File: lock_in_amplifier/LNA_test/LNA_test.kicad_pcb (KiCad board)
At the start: 2 copper layers, 22.1 x 17.8 mm, 111 parts, among them J1 vref-in, J10 A IN, J11 B IN, J12 POWER_IN, J15 I IN, J17 RF_Shield_One_Piece, J19 +3V3 OUT, J2 vref, J20 AMP OUT, J3 V-IN, J38 RF_Shield_One_Piece, J4 GND, J46 -5V OUT, J47 +5V OUT, J5 V+IN, J6 +5V, J7 +3V3, J8 -5V, Q1 DMN640L, Q2 DMN640L, U1 LM833, U2 lm7805, U3 LM7833, U4 lm7905, U6 lmp7721, U7 LM833, U8 AD8429

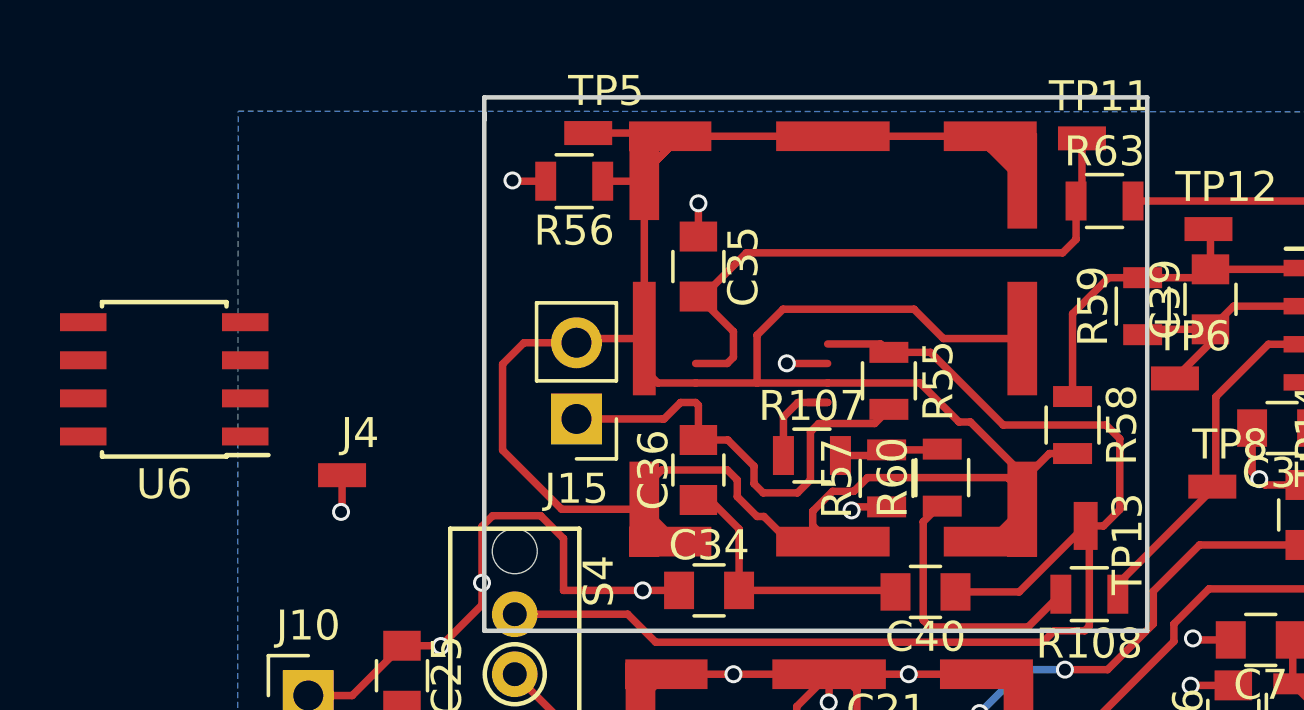
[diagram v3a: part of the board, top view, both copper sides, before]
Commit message: finished relayout of tia - soic
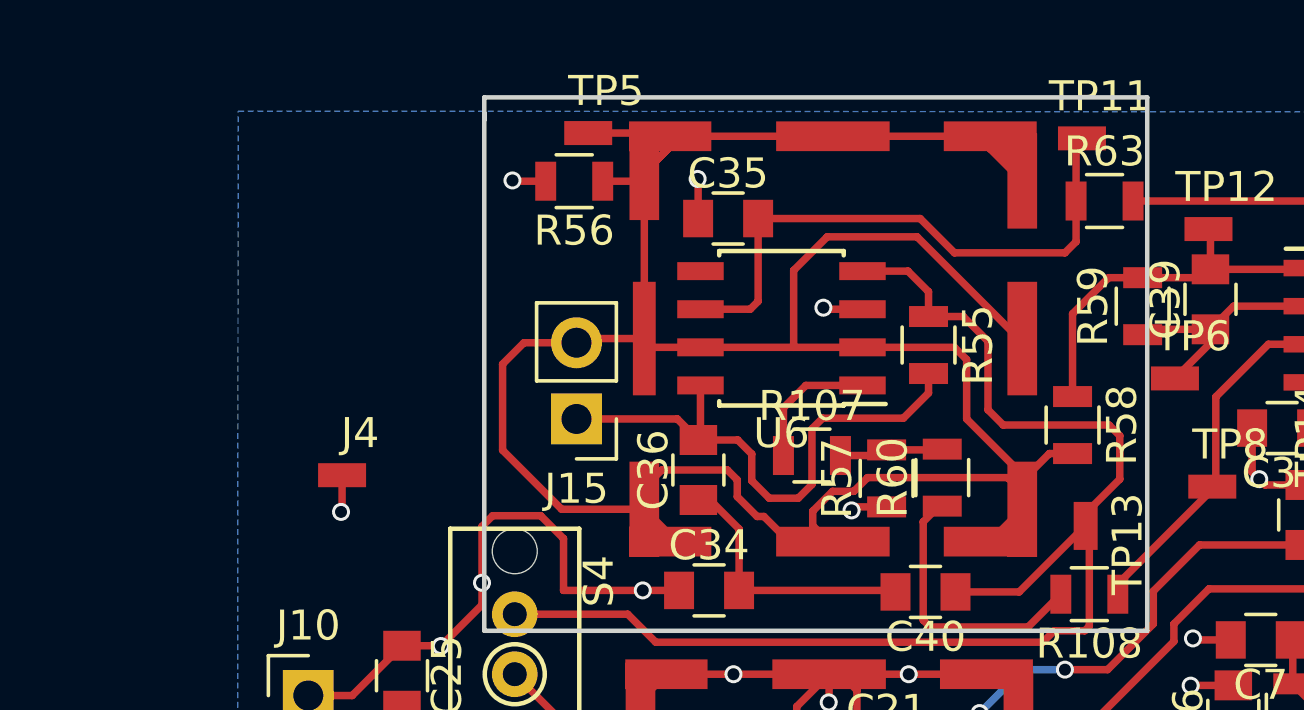
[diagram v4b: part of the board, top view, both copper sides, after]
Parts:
- moved U6 20.6 mm to (101.1, 70.4)
- moved C35 1.88 mm to (99.3, 66.8), turned to 0 degrees
- moved R55 1.78 mm to (106.0, 71.0)
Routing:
- net /sheet5A330123/GUARD: track 96.7 -> 101.8 mm
- net /sheet5A330123/I_IN: track 15.6 -> 18.7 mm
- net Net-(C40-Pad1): track 43.4 -> 44.8 mm
- net (no net): track 1.36 -> 0.00 mm, vias 1 -> 0
- net Net-(C35-Pad2): track 20.8 -> 19.5 mm
- net GND: track 173.1 -> 174.4 mm, vias 45 -> 46
- net Net-(R107-Pad1): track 3.63 -> 4.53 mm

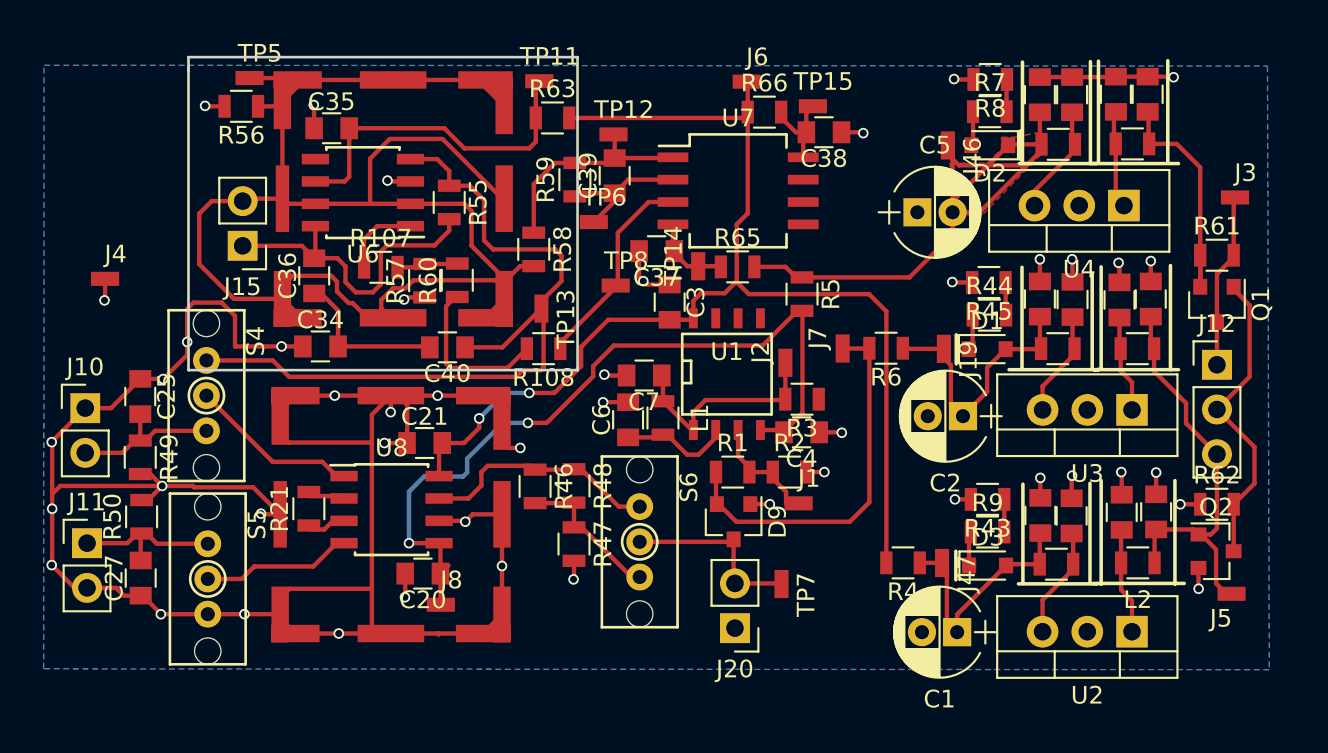
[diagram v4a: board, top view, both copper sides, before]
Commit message: silkscreen readability changes
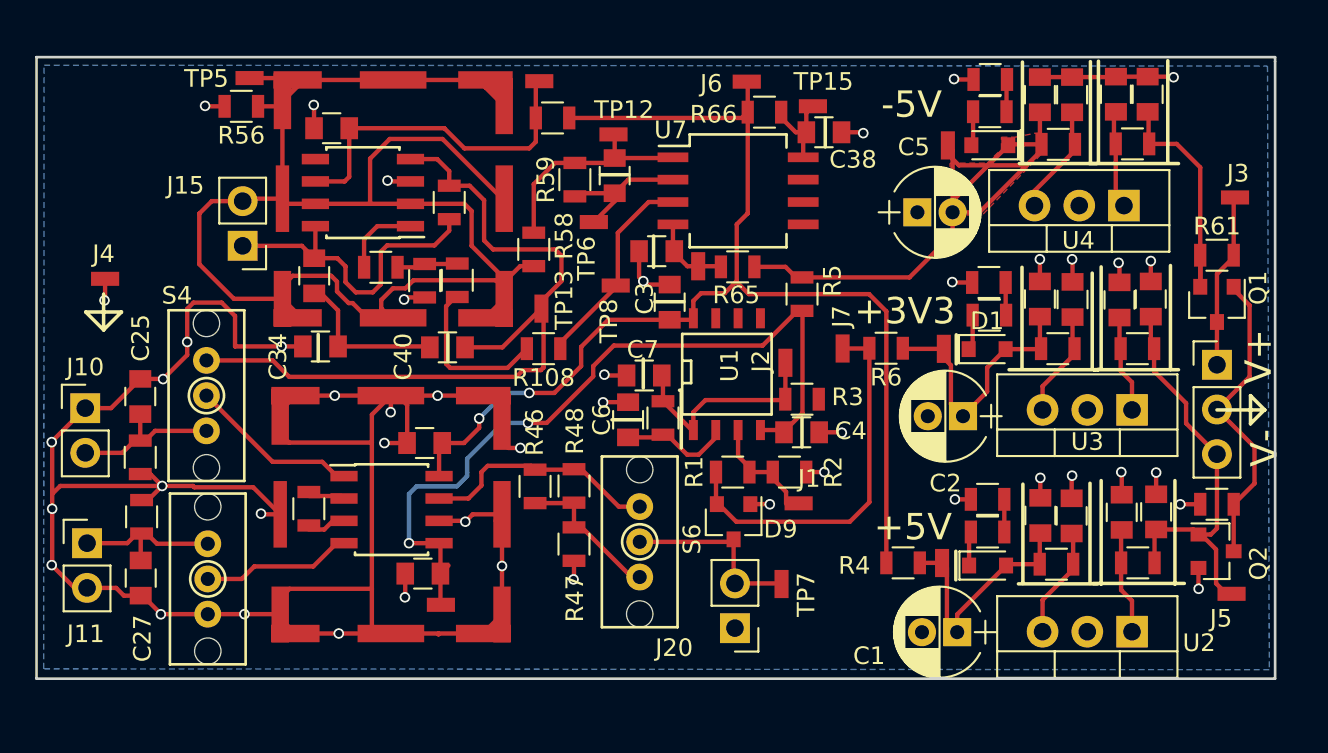
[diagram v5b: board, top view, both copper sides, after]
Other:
- board size 22.1 x 17.8 mm -> 70.4 x 35.3 mm
- board text added: "+3V3"
- board text added: "+5V"
- board text added: "-5V"
- board text added: "V+"
- board text added: "V-"

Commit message: misc debug
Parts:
- removed C34: 200pF, Capacitors_SMD:C_0805
- removed C40: 10pF, Capacitors_SMD:C_0805
- removed R107: 0, Resistors_SMD:R_0805
- added R64: 100, Resistors_SMD:R_0805, F.Cu at (98.5, 74.4)
- added REF**: MountingHole_2.2mm_M2, Mounting_Holes:MountingHole_2.2mm_M2, F.Cu at (149.9, 95.2)
- added REF**: MountingHole_2.2mm_M2, Mounting_Holes:MountingHole_2.2mm_M2, F.Cu at (149.9, 66.0)
- added REF**: MountingHole_2.2mm_M2, Mounting_Holes:MountingHole_2.2mm_M2, F.Cu at (86.4, 66.0)
- added REF***: OSHW-Logo2_7.3x6mm_SilkScreen, Symbols:OSHW-Logo2_7.3x6mm_SilkScreen, F.Cu at (86.5, 71.6)
- R55: value 1M -> 100M
- moved TP13 16.6 mm to (96.5, 78.0), turned to 0 degrees
- moved J5 6.23 mm to (153.9, 90.4), turned to 270 degrees
- moved R108 5.89 mm to (113.7, 73.9)
- moved R55 5.17 mm to (101.5, 73.5), turned to 180 degrees
- moved C36 3.19 mm to (101.5, 75.4), turned to 180 degrees
- moved R60 2.25 mm to (105.3, 73.5), turned to 180 degrees
- moved C35 1.05 mm to (99.6, 65.8)
- moved U6 0.92 mm to (101.2, 69.5)
- moved R57 0.71 mm to (105.3, 75.5), turned to 180 degrees
- moved TP8 0.69 mm to (115.4, 73.8)
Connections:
- C36 pad 1: Net-(C34-Pad2) -> Net-(C36-Pad1)
- C36 pad 2: /sheet5A330123/I_IN -> Net-(C36-Pad2)
- R55 pad 1: Net-(C40-Pad1) -> Net-(C36-Pad1)
- R55 pad 2: /sheet5A330123/I_IN -> Net-(C36-Pad2)
- R57 pad 2: Net-(R107-Pad2) -> Net-(R57-Pad2)
- R60 pad 2: Net-(R107-Pad2) -> Net-(R57-Pad2)
- S4 pad 1: Net-(C40-Pad1) -> Net-(C36-Pad1)
- TP13 pad 1: Net-(C40-Pad1) -> Net-(C36-Pad1)
- U6 pad 1: Net-(R107-Pad1) -> Net-(R57-Pad2)
- U6 pad 4: Net-(C40-Pad1) -> Net-(C36-Pad1)
- U6 pad 8: /sheet5A330123/I_IN -> Net-(C36-Pad2)
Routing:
- net /sheet5A330123/GUARD: track 101.8 -> 146.7 mm, vias 0 -> 13
- net Net-(C40-Pad1): track 44.8 -> 0.00 mm
- net Net-(C36-Pad1): track 0.00 -> 26.8 mm
- net /sheet5A330123/I_IN: track 18.7 -> 5.36 mm
- net Net-(C34-Pad2): track 9.66 -> 0.00 mm
- net GND: track 174.4 -> 165.9 mm, vias 46 -> 45
- net Net-(C36-Pad2): track 0.00 -> 6.02 mm
- net Net-(R108-Pad1): track 12.9 -> 7.20 mm
- net Net-(R107-Pad1): track 4.53 -> 0.00 mm
- net Net-(R57-Pad2): track 0.00 -> 4.29 mm
- net Net-(R107-Pad2): track 3.48 -> 0.00 mm
- net Net-(R108-Pad2): track 9.61 -> 6.70 mm
- net /sheet5A330121/V+_IN: track 23.6 -> 26.4 mm
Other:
- board text added: "LMP7721 TIA"
- board text added: "LNA TEST BOARD V 1.0 LMP7721 TIA / GUARD DRIVE AD8429 INST. AMP. +5,-5,+3V3 REG. SUPPLY 1.65V REF. DRIVE. GPL V3.0"
- board text removed: "CAREFUL OF GROUNDING - TIA"
- board text removed: "check lmp7721 package! gawd I hope I don't have to re-lay that"
